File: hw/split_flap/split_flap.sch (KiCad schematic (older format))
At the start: 7 parts, among them J15 MOTOR_POWER, J16 JUMPER_MOTOR_5V, J17 EXPANDER_PORT, J19 POWER, U1 74HCT125, U2 NodeMCU_1.0_(ESP-12E)

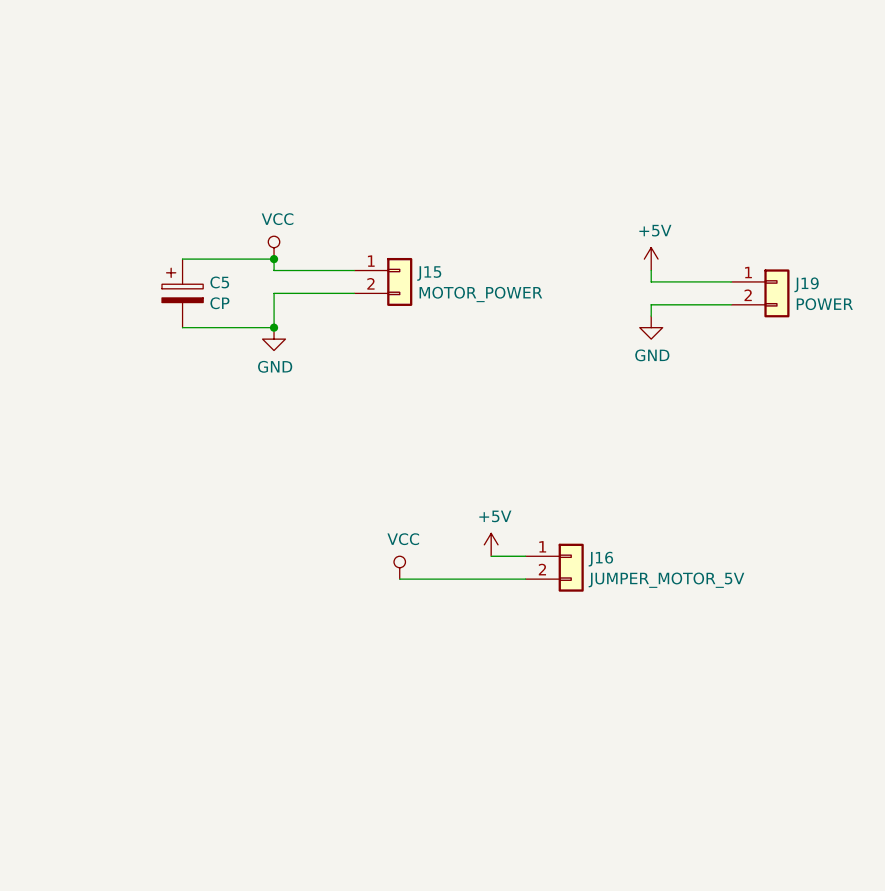
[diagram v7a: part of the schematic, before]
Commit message: Add mounting holes, logo and capacitor for +5V
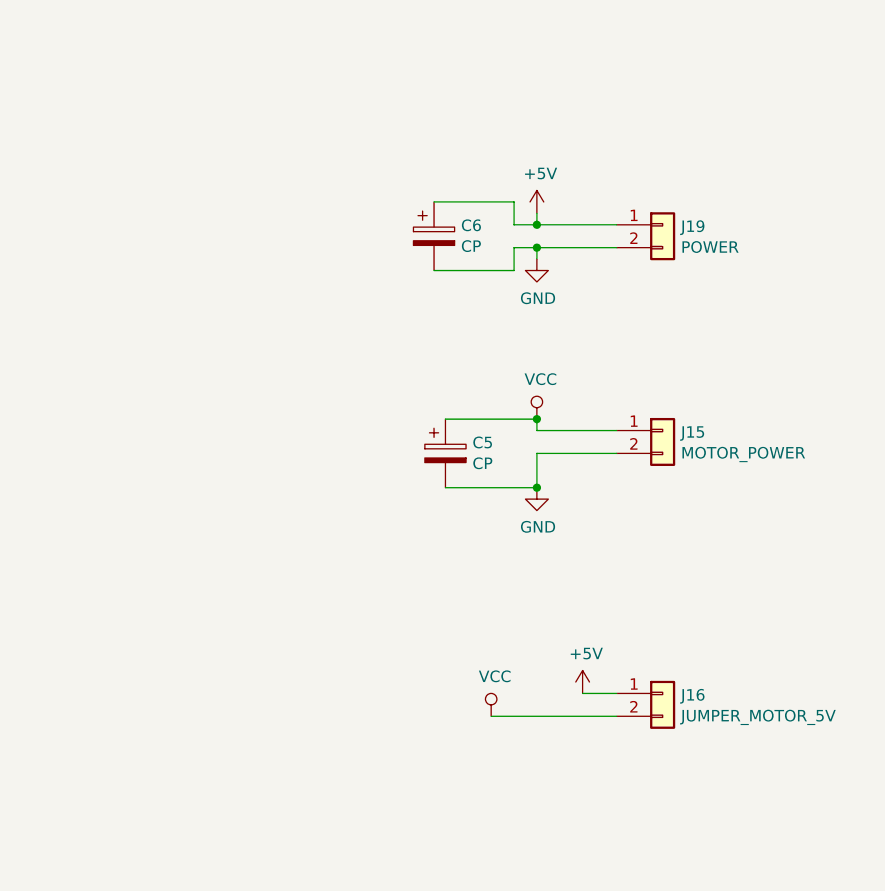
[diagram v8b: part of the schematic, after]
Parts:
- added C6: CP, Capacitor_THT:CP_Radial_D6.3mm_P2.50mm, symbol Device:CP
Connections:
- net +5V: now also C6.1
- net GND: now also C6.2
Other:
- moved on the sheet: C5, J15, J16, J19
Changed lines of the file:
@@
 L Connector_Generic:Conn_01x02 J19
 U 1 1 5E33CF31
-P 10400 4300
-F 0 "J19" H 10480 4292 50  0000 L CNN
-F 1 "POWER" H 10480 4201 50  0000 L CNN
-F 2 "Connector_JST:JST_XH_B2B-XH-A_1x02_P2.50mm_Vertical" H 10400 4300 50  0001 C CNN
-F 3 "~" H 10400 4300 50  0001 C CNN
-	1    10400 4300
+P 9900 4050
+F 0 "J19" H 9980 4042 50  0000 L CNN
+F 1 "POWER" H 9980 3951 50  0000 L CNN
+F 2 "Connector_JST:JST_XH_B2B-XH-A_1x02_P2.50mm_Vertical" H 9900 4050 50  0001 C CNN
+F 3 "~" H 9900 4050 50  0001 C CNN
+	1    9900 4050
 	1    0    0    -1
 $EndComp
@@
 L power:GND #PWR023
 U 1 1 5E33E103
-P 9850 4450
-F 0 "#PWR023" H 9850 4200 50  0001 C CNN
-F 1 "GND" H 9855 4277 50  0000 C CNN
-F 2 "" H 9850 4450 50  0001 C CNN
-F 3 "" H 9850 4450 50  0001 C CNN
-	1    9850 4450
-	1    0    0    -1
-$EndComp
-Wire Wire Line
-	10200 4300 9850 4300
-Wire Wire Line
-	9850 4300 9850 4250
-Wire Wire Line
-	9850 4450 9850 4400
-Wire Wire Line
-	9850 4400 10200 4400
+P 9350 4200
+F 0 "#PWR023" H 9350 3950 50  0001 C CNN
+F 1 "GND" H 9355 4027 50  0000 C CNN
+F 2 "" H 9350 4200 50  0001 C CNN
+F 3 "" H 9350 4200 50  0001 C CNN
+	1    9350 4200
+	1    0    0    -1
+$EndComp
+Wire Wire Line
+	9700 4050 9350 4050
+Wire Wire Line
+	9350 4050 9350 4000
+Wire Wire Line
+	9350 4200 9350 4150
 $Comp
 L power:GND #PWR0144
@@
 L power:+5V #PWR022
 U 1 1 5E33DBA2
-P 9850 4250
-F 0 "#PWR022" H 9850 4100 50  0001 C CNN
-F 1 "+5V" H 9865 4423 50  0000 C CNN
-F 2 "" H 9850 4250 50  0001 C CNN
-F 3 "" H 9850 4250 50  0001 C CNN
-	1    9850 4250
+P 9350 4000
+F 0 "#PWR022" H 9350 3850 50  0001 C CNN
+F 1 "+5V" H 9365 4173 50  0000 C CNN
+F 2 "" H 9350 4000 50  0001 C CNN
+F 3 "" H 9350 4000 50  0001 C CNN
+	1    9350 4000
 	1    0    0    -1
 $EndComp
@@
 L Connector_Generic:Conn_01x02 J15
 U 1 1 5DF8E830
-P 8750 4250
-F 0 "J15" H 8830 4242 50  0000 L CNN
-F 1 "MOTOR_POWER" H 8830 4151 50  0000 L CNN
-F 2 "Connector_JST:JST_XH_B2B-XH-A_1x02_P2.50mm_Vertical" H 8750 4250 50  0001 C CNN
-F 3 "~" H 8750 4250 50  0001 C CNN
-	1    8750 4250
+P 9900 4950
+F 0 "J15" H 9980 4942 50  0000 L CNN
+F 1 "MOTOR_POWER" H 9980 4851 50  0000 L CNN
+F 2 "Connector_JST:JST_XH_B2B-XH-A_1x02_P2.50mm_Vertical" H 9900 4950 50  0001 C CNN
+F 3 "~" H 9900 4950 50  0001 C CNN
+	1    9900 4950
 	1    0    0    -1
 $EndComp
@@
 L power:GND #PWR036
 U 1 1 5DF8E83A
-P 8200 4500
-F 0 "#PWR036" H 8200 4250 50  0001 C CNN
-F 1 "GND" H 8205 4327 50  0000 C CNN
-F 2 "" H 8200 4500 50  0001 C CNN
-F 3 "" H 8200 4500 50  0001 C CNN
-	1    8200 4500
-	1    0    0    -1
-$EndComp
-Wire Wire Line
-	8550 4250 8200 4250
-Wire Wire Line
-	8200 4250 8200 4200
-Wire Wire Line
-	8200 4500 8200 4350
-Wire Wire Line
-	8200 4350 8550 4350
+P 9350 5200
+F 0 "#PWR036" H 9350 4950 50  0001 C CNN
+F 1 "GND" H 9355 5027 50  0000 C CNN
+F 2 "" H 9350 5200 50  0001 C CNN
+F 3 "" H 9350 5200 50  0001 C CNN
+	1    9350 5200
+	1    0    0    -1
+$EndComp
+Wire Wire Line
+	9700 4950 9350 4950
+Wire Wire Line
+	9350 4950 9350 4900
+Wire Wire Line
+	9350 5200 9350 5050
+Wire Wire Line
+	9350 5050 9700 5050
 $Comp
 L power:VCC #PWR07
 U 1 1 5DF91957
-P 8200 4200
-F 0 "#PWR07" H 8200 4050 50  0001 C CNN
-F 1 "VCC" H 8217 4373 50  0000 C CNN
-F 2 "" H 8200 4200 50  0001 C CNN
-F 3 "" H 8200 4200 50  0001 C CNN
-	1    8200 4200
+P 9350 4900
+F 0 "#PWR07" H 9350 4750 50  0001 C CNN
+F 1 "VCC" H 9367 5073 50  0000 C CNN
+F 2 "" H 9350 4900 50  0001 C CNN
+F 3 "" H 9350 4900 50  0001 C CNN
+	1    9350 4900
 	1    0    0    -1
 $EndComp
@@
 L Device:CP C5
 U 1 1 5DF927D9
-P 7800 4350
-F 0 "C5" H 7918 4396 50  0000 L CNN
-F 1 "CP" H 7918 4305 50  0000 L CNN
-F 2 "Capacitor_THT:CP_Radial_D6.3mm_P2.50mm" H 7838 4200 50  0001 C CNN
-F 3 "~" H 7800 4350 50  0001 C CNN
-	1    7800 4350
-	1    0    0    -1
-$EndComp
-Wire Wire Line
-	8200 4200 7800 4200
-Connection ~ 8200 4200
-Wire Wire Line
-	7800 4500 8200 4500
-Connection ~ 8200 4500
+P 8950 5050
+F 0 "C5" H 9068 5096 50  0000 L CNN
+F 1 "CP" H 9068 5005 50  0000 L CNN
+F 2 "Capacitor_THT:CP_Radial_D6.3mm_P2.50mm" H 8988 4900 50  0001 C CNN
+F 3 "~" H 8950 5050 50  0001 C CNN
+	1    8950 5050
+	1    0    0    -1
+$EndComp
+Wire Wire Line
+	9350 4900 8950 4900
+Connection ~ 9350 4900
+Wire Wire Line
+	8950 5200 9350 5200
+Connection ~ 9350 5200
 $Comp
 L Connector_Generic:Conn_01x02 J16
 U 1 1 5DFA08C7
-P 9500 5500
-F 0 "J16" H 9580 5492 50  0000 L CNN
-F 1 "JUMPER_MOTOR_5V" H 9580 5401 50  0000 L CNN
-F 2 "Connector_PinHeader_2.54mm:PinHeader_1x02_P2.54mm_Vertical" H 9500 5500 50  0001 C CNN
-F 3 "~" H 9500 5500 50  0001 C CNN
-	1    9500 5500
+P 9900 6100
+F 0 "J16" H 9980 6092 50  0000 L CNN
+F 1 "JUMPER_MOTOR_5V" H 9980 6001 50  0000 L CNN
+F 2 "Connector_PinHeader_2.54mm:PinHeader_1x02_P2.54mm_Vertical" H 9900 6100 50  0001 C CNN
+F 3 "~" H 9900 6100 50  0001 C CNN
+	1    9900 6100
 	1    0    0    -1
 $EndComp
@@
 L power:+5V #PWR038
 U 1 1 5DFA2C17
-P 9150 5500
-F 0 "#PWR038" H 9150 5350 50  0001 C CNN
-F 1 "+5V" H 9165 5673 50  0000 C CNN
-F 2 "" H 9150 5500 50  0001 C CNN
-F 3 "" H 9150 5500 50  0001 C CNN
-	1    9150 5500
+P 9550 6100
+F 0 "#PWR038" H 9550 5950 50  0001 C CNN
+F 1 "+5V" H 9565 6273 50  0000 C CNN
+F 2 "" H 9550 6100 50  0001 C CNN
+F 3 "" H 9550 6100 50  0001 C CNN
+	1    9550 6100
 	1    0    0    -1
 $EndComp
@@
 L power:VCC #PWR037
 U 1 1 5DFC9FF1
-P 8750 5600
-F 0 "#PWR037" H 8750 5450 50  0001 C CNN
-F 1 "VCC" H 8767 5773 50  0000 C CNN
-F 2 "" H 8750 5600 50  0001 C CNN
-F 3 "" H 8750 5600 50  0001 C CNN
-	1    8750 5600
-	1    0    0    -1
-$EndComp
-Wire Wire Line
-	9300 5500 9150 5500
-Wire Wire Line
-	8750 5600 9300 5600
+P 9150 6200
+F 0 "#PWR037" H 9150 6050 50  0001 C CNN
+F 1 "VCC" H 9167 6373 50  0000 C CNN
+F 2 "" H 9150 6200 50  0001 C CNN
+F 3 "" H 9150 6200 50  0001 C CNN
+	1    9150 6200
+	1    0    0    -1
+$EndComp
+Wire Wire Line
+	9700 6100 9550 6100
+Wire Wire Line
+	9150 6200 9700 6200
 Wire Wire Line
 	9150 2450 8550 2450
@@
 Wire Wire Line
 	9650 2250 9850 2250
+$Comp
+L Device:CP C6
+U 1 1 5DFAE59C
+P 8900 4100
+F 0 "C6" H 9018 4146 50  0000 L CNN
+F 1 "CP" H 9018 4055 50  0000 L CNN
+F 2 "Capacitor_THT:CP_Radial_D6.3mm_P2.50mm" H 8938 3950 50  0001 C CNN
+F 3 "~" H 8900 4100 50  0001 C CNN
+	1    8900 4100
+	1    0    0    -1
+$EndComp
+Wire Wire Line
+	8900 3950 9250 3950
+Wire Wire Line
+	9250 3950 9250 4050
+Wire Wire Line
+	9250 4050 9350 4050
+Connection ~ 9350 4050
+Wire Wire Line
+	8900 4250 9250 4250
+Wire Wire Line
+	9250 4250 9250 4150
+Wire Wire Line
+	9250 4150 9350 4150
+Connection ~ 9350 4150
+Wire Wire Line
+	9350 4150 9700 4150
 $EndSCHEMATC
